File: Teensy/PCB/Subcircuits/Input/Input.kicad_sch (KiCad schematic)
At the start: 4 parts

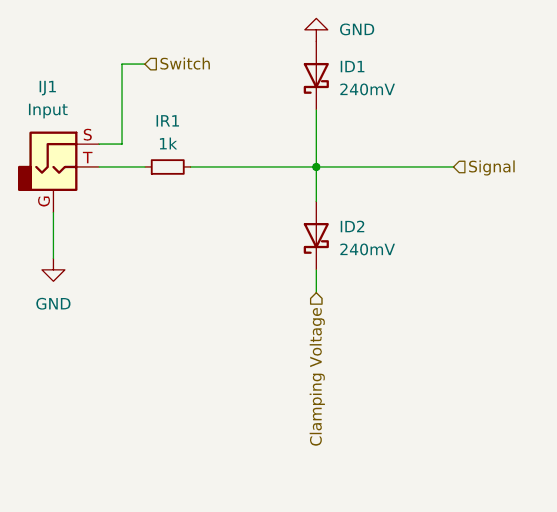
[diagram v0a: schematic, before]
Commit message: Added USB_IO module PCB
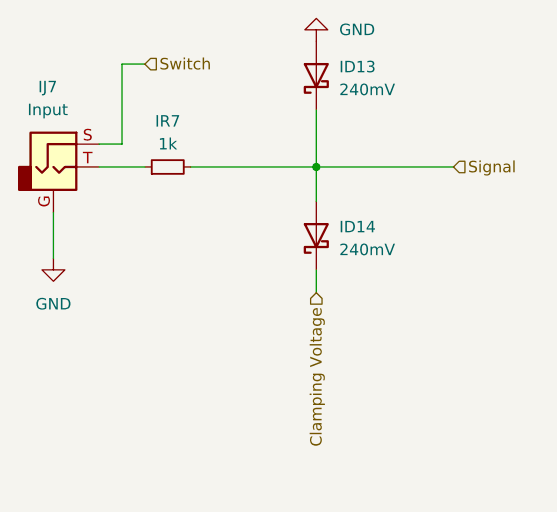
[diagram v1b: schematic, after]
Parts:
- renumbered ID1 to ID13, ID2 to ID14, IJ1 to IJ7, IR1 to IR7
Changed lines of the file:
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@@
   (symbol (lib_id "Connector:AudioJack2_Ground") (at 52.07 62.23 0) (unit 1)
     (in_bom yes) (on_board yes) (fields_autoplaced)
-    (property "Reference" "IJ1" (id 0) (at 51.435 53.34 0))
+    (property "Reference" "IJ7" (id 0) (at 51.435 53.34 0))
     (property "Value" "Input" (id 1) (at 51.435 55.88 0))
     (property "Footprint" "Perfboard:3.5mm Jack Perfboard" (id 2) (at 52.07 62.23 0)
@@
   (symbol (lib_id "Device:D_Schottky") (at 81.28 69.85 90) (unit 1)
     (in_bom yes) (on_board yes) (fields_autoplaced)
-    (property "Reference" "ID2" (id 0) (at 83.82 68.8974 90)
+    (property "Reference" "ID14" (id 0) (at 83.82 68.8974 90)
       (effects (font (size 1.27 1.27)) (justify right))
     )
@@
   (symbol (lib_id "power:GND") (at 52.07 72.39 0) (unit 1)
     (in_bom yes) (on_board yes) (fields_autoplaced)
-    (property "Reference" "#PWR022" (id 0) (at 52.07 78.74 0)
+    (property "Reference" "#PWR0146" (id 0) (at 52.07 78.74 0)
       (effects (font (size 1.27 1.27)) hide)
     )
@@
   (symbol (lib_id "power:GND") (at 81.28 48.26 180) (unit 1)
     (in_bom yes) (on_board yes) (fields_autoplaced)
-    (property "Reference" "#PWR023" (id 0) (at 81.28 41.91 0)
+    (property "Reference" "#PWR0145" (id 0) (at 81.28 41.91 0)
       (effects (font (size 1.27 1.27)) hide)
     )
@@
   (symbol (lib_id "Device:R_Small") (at 64.77 62.23 90) (unit 1)
     (in_bom yes) (on_board yes)
-    (property "Reference" "IR1" (id 0) (at 64.77 57.15 90))
+    (property "Reference" "IR7" (id 0) (at 64.77 57.15 90))
     (property "Value" "1k" (id 1) (at 64.77 59.69 90))
     (property "Footprint" "Resistor_SMD:R_1206_3216Metric_Pad1.30x1.75mm_HandSolder" (id 2) (at 64.77 62.23 0)
@@
   (symbol (lib_id "Device:D_Schottky") (at 81.28 52.07 90) (unit 1)
     (in_bom yes) (on_board yes) (fields_autoplaced)
-    (property "Reference" "ID1" (id 0) (at 83.82 51.1174 90)
+    (property "Reference" "ID13" (id 0) (at 83.82 51.1174 90)
       (effects (font (size 1.27 1.27)) (justify right))
     )

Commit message: Replaced Schematic Lines with references
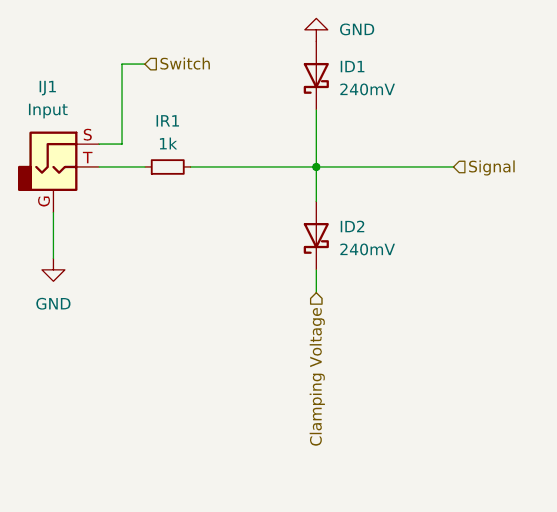
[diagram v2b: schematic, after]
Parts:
- renumbered ID13 to ID1, ID14 to ID2, IJ7 to IJ1, IR7 to IR1
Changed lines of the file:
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@@
   (symbol (lib_id "Connector:AudioJack2_Ground") (at 52.07 62.23 0) (unit 1)
     (in_bom yes) (on_board yes) (fields_autoplaced)
-    (property "Reference" "IJ7" (id 0) (at 51.435 53.34 0))
+    (property "Reference" "IJ1" (id 0) (at 51.435 53.34 0))
     (property "Value" "Input" (id 1) (at 51.435 55.88 0))
     (property "Footprint" "Perfboard:3.5mm Jack Perfboard" (id 2) (at 52.07 62.23 0)
@@
   (symbol (lib_id "Device:D_Schottky") (at 81.28 69.85 90) (unit 1)
     (in_bom yes) (on_board yes) (fields_autoplaced)
-    (property "Reference" "ID14" (id 0) (at 83.82 68.8974 90)
+    (property "Reference" "ID2" (id 0) (at 83.82 68.8974 90)
       (effects (font (size 1.27 1.27)) (justify right))
     )
@@
   (symbol (lib_id "power:GND") (at 52.07 72.39 0) (unit 1)
     (in_bom yes) (on_board yes) (fields_autoplaced)
-    (property "Reference" "#PWR0146" (id 0) (at 52.07 78.74 0)
+    (property "Reference" "#PWR022" (id 0) (at 52.07 78.74 0)
       (effects (font (size 1.27 1.27)) hide)
     )
@@
   (symbol (lib_id "power:GND") (at 81.28 48.26 180) (unit 1)
     (in_bom yes) (on_board yes) (fields_autoplaced)
-    (property "Reference" "#PWR0145" (id 0) (at 81.28 41.91 0)
+    (property "Reference" "#PWR023" (id 0) (at 81.28 41.91 0)
       (effects (font (size 1.27 1.27)) hide)
     )
@@
   (symbol (lib_id "Device:R_Small") (at 64.77 62.23 90) (unit 1)
     (in_bom yes) (on_board yes)
-    (property "Reference" "IR7" (id 0) (at 64.77 57.15 90))
+    (property "Reference" "IR1" (id 0) (at 64.77 57.15 90))
     (property "Value" "1k" (id 1) (at 64.77 59.69 90))
     (property "Footprint" "Resistor_SMD:R_1206_3216Metric_Pad1.30x1.75mm_HandSolder" (id 2) (at 64.77 62.23 0)
@@
   (symbol (lib_id "Device:D_Schottky") (at 81.28 52.07 90) (unit 1)
     (in_bom yes) (on_board yes) (fields_autoplaced)
-    (property "Reference" "ID13" (id 0) (at 83.82 51.1174 90)
+    (property "Reference" "ID1" (id 0) (at 83.82 51.1174 90)
       (effects (font (size 1.27 1.27)) (justify right))
     )
